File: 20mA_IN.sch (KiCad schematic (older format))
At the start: 10 parts, among them U5 PC817, U6 PC817, U7 LM321

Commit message: Op amp power supply in 20mA_IN switched to 5V
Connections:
- net 24V is gone; now on net 5V: U7.5 (V+)
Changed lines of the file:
@@
 $Descr A4 11693 8268
 encoding utf-8
-Sheet 5 5
+Sheet 4 5
 Title ""
 Date ""
@@
 	6500 4850 6500 4700
 Connection ~ 5950 4850
-Text GLabel 6400 3850 0    50   Input ~ 0
-24V
-Wire Wire Line
-	6400 3850 6500 3850
 Wire Wire Line
 	6500 3850 6500 4100
@@
 	8000 3550 8550 3550
 Connection ~ 8000 3550
+Wire Wire Line
+	5700 3350 5700 3850
+Wire Wire Line
+	5700 3850 6500 3850
 $EndSCHEMATC

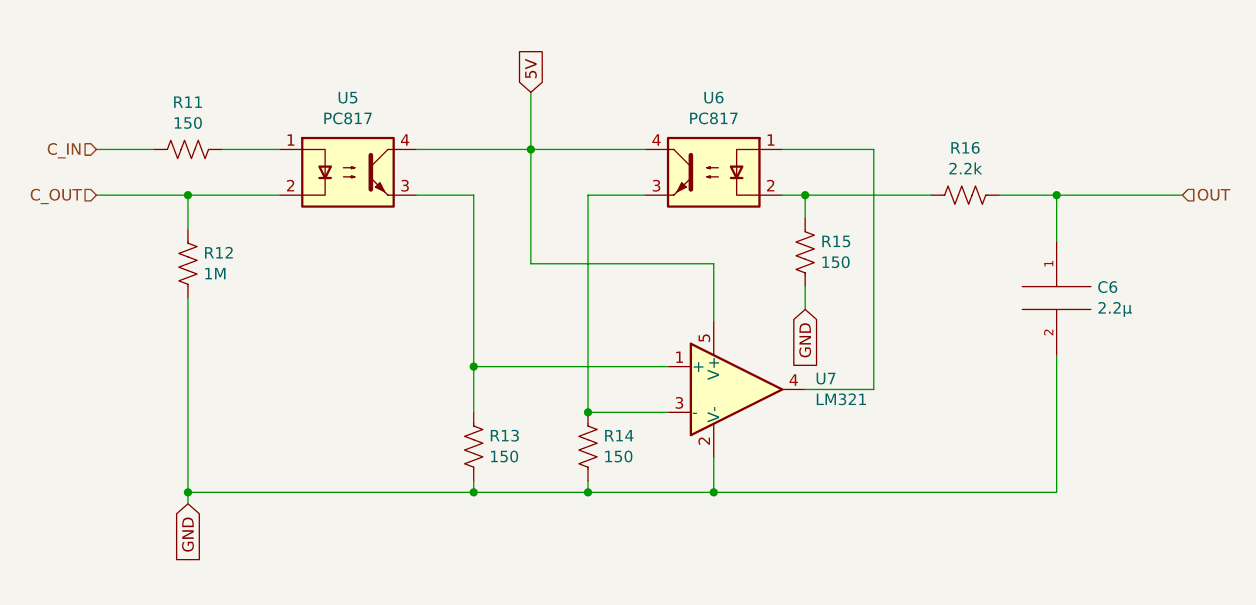
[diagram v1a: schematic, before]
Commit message: Previous current input circuit was reaching op amp saturation. Possible solution may involve transistor, but for now, higher power supply is sufficient.
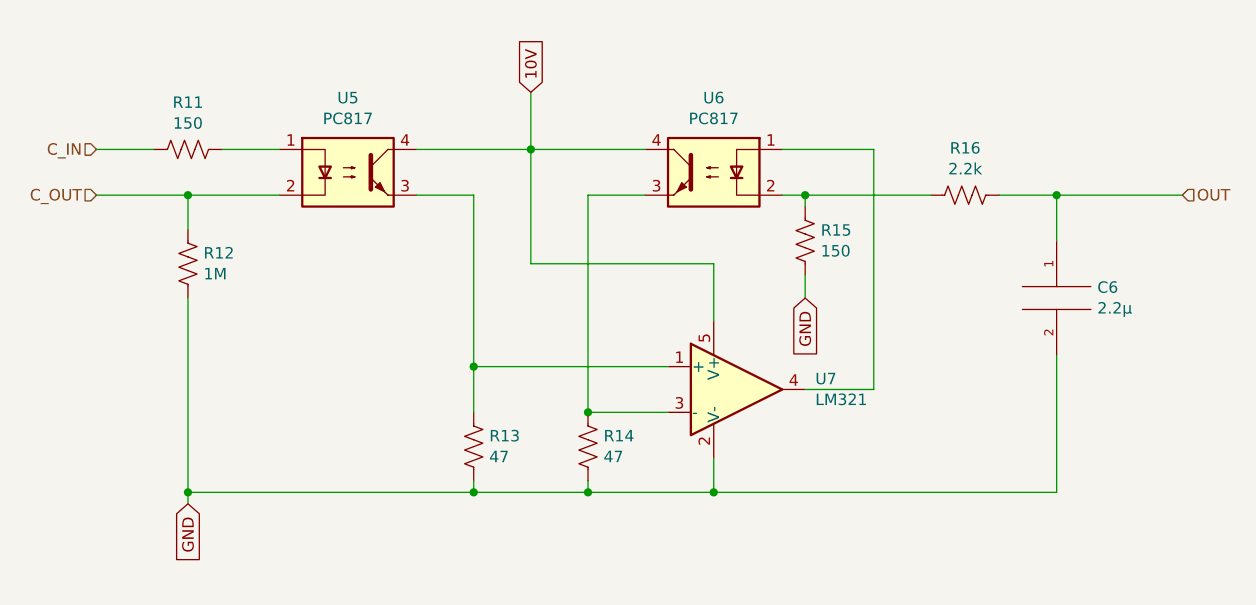
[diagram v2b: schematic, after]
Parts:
- R13, R14: value 150 -> 47
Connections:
- net 5V renamed 10V
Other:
- moved on the sheet: R15
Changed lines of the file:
@@
 P 5950 4650
 F 0 "R14" H 5882 4604 50  0000 R CNN
-F 1 "150" H 5882 4695 50  0000 R CNN
+F 1 "47" H 5882 4695 50  0000 R CNN
 F 2 "" V 5990 4640 50  0001 C CNN
 F 3 "~" H 5950 4650 50  0001 C CNN
@@
 P 5450 4650
 F 0 "R13" H 5382 4604 50  0000 R CNN
-F 1 "150" H 5382 4695 50  0000 R CNN
+F 1 "47" H 5382 4695 50  0000 R CNN
 F 2 "" V 5490 4640 50  0001 C CNN
 F 3 "~" H 5450 4650 50  0001 C CNN
@@
 	4200 4850 4200 4000
 Text GLabel 5700 3100 1    50   Input ~ 0
-5V
+10V
 Wire Wire Line
 	5700 3350 6200 3350
@@
 Wire Wire Line
 	5700 3100 5700 3350
-Wire Wire Line
-	6900 4400 7200 4400
-Wire Wire Line
-	7200 4400 7200 3350
-Wire Wire Line
-	7200 3350 6800 3350
-Text GLabel 6900 4050 3    50   Input ~ 0
+Text GLabel 6900 4000 3    50   Input ~ 0
 GND
-Wire Wire Line
-	6900 3950 6900 4050
-Wire Wire Line
-	6800 3550 6900 3550
-Wire Wire Line
-	6900 3550 6900 3650
 Wire Wire Line
 	5950 4850 6500 4850
@@
 L Device:R_US R15
 U 1 1 60AD8205
-P 6900 3800
-F 0 "R15" H 6832 3754 50  0000 R CNN
-F 1 "150" H 6832 3845 50  0000 R CNN
-F 2 "" V 6940 3790 50  0001 C CNN
-F 3 "~" H 6900 3800 50  0001 C CNN
-	1    6900 3800
+P 6900 3750
+F 0 "R15" H 6832 3704 50  0000 R CNN
+F 1 "150" H 6832 3795 50  0000 R CNN
+F 2 "" V 6940 3740 50  0001 C CNN
+F 3 "~" H 6900 3750 50  0001 C CNN
+	1    6900 3750
 	-1   0    0    1
 $EndComp
@@
 $EndComp
 Wire Wire Line
-	6900 3550 7450 3550
-Connection ~ 6900 3550
-Wire Wire Line
 	7750 3550 8000 3550
 Wire Wire Line
@@
 Wire Wire Line
 	5700 3850 6500 3850
+Wire Wire Line
+	6800 3550 6900 3550
+Wire Wire Line
+	6900 3550 6900 3600
+Connection ~ 6900 3550
+Wire Wire Line
+	6900 3550 7450 3550
+Wire Wire Line
+	6900 4400 7200 4400
+Wire Wire Line
+	7200 4400 7200 3350
+Wire Wire Line
+	7200 3350 6800 3350
+Wire Wire Line
+	6900 3900 6900 4000
 $EndSCHEMATC

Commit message: Added Optically Isolated Digital Input
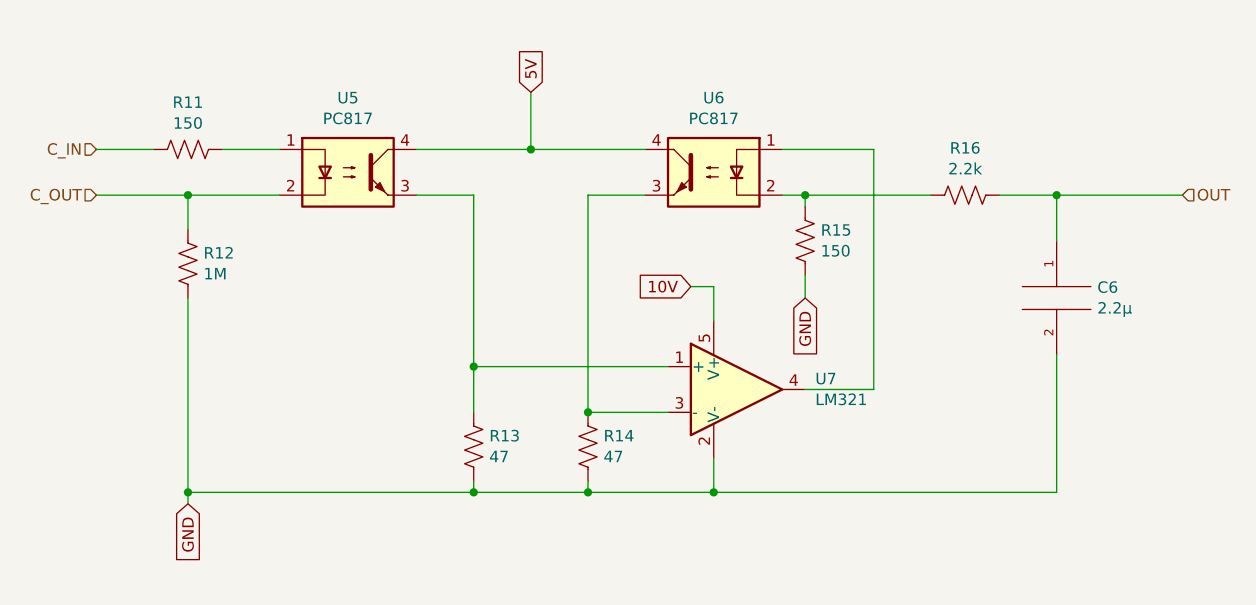
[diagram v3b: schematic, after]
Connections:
- net 10V: no longer U5.4, U6.4
- new net 5V: U5.4, U6.4
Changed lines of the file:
@@
 $Descr A4 11693 8268
 encoding utf-8
-Sheet 4 5
+Sheet 5 6
 Title ""
 Date ""
@@
 	4200 4850 4200 4000
 Text GLabel 5700 3100 1    50   Input ~ 0
-10V
+5V
 Wire Wire Line
 	5700 3350 6200 3350
@@
 	6500 4850 6500 4700
 Connection ~ 5950 4850
-Wire Wire Line
-	6500 3850 6500 4100
 $Comp
 L Device:R_US R15
@@
 Connection ~ 8000 3550
 Wire Wire Line
-	5700 3350 5700 3850
-Wire Wire Line
-	5700 3850 6500 3850
-Wire Wire Line
 	6800 3550 6900 3550
 Wire Wire Line
@@
 Wire Wire Line
 	6900 3900 6900 4000
+Text GLabel 6400 3950 0    50   Input ~ 0
+10V
+Wire Wire Line
+	6400 3950 6500 3950
+Wire Wire Line
+	6500 3950 6500 4100
 $EndSCHEMATC

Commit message: Comments and Notation for clarity
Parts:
- added Q?: S8050, Package_TO_SOT_THT:TO-92_Inline, symbol Transistor_BJT:S8050
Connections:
- net 10V is gone; now on net 5V: U7.5 (V+)
- net 5V: now also Q?.3 (C)
- net at U6.1: now also Q?.1 (E); no longer U7.4
- new net: Q?.2 (B), U7.4
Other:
- note added: "1st Order Low Pass Filter"
- note added: "Since V over R13 = V over R14 by presence of U7, I into U5 = I into U6"
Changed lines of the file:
@@
 encoding utf-8
 Sheet 5 6
-Title ""
-Date ""
-Rev ""
-Comp ""
-Comment1 ""
+Title "20mA to 3.3V Input"
+Date "2021-05-25"
+Rev "1"
+Comp "Harsch Systems"
+Comment1 "Tyler Stowell"
 Comment2 ""
 Comment3 ""
@@
 $EndComp
 $Comp
-L Amplifier_Operational:LM321 U?
-U 1 1 60ACD8A3
-P 6600 4400
-AR Path="/60A68B69/60ACD8A3" Ref="U?"  Part="1"
-AR Path="/60A8EFC5/60ACD8A3" Ref="U?"  Part="1"
-AR Path="/60AC3F67/60ACD8A3" Ref="U7"  Part="1"
-F 0 "U7" H 6944 4446 50  0000 L CNN
-F 1 "LM321" H 6944 4355 50  0000 L CNN
-F 2 "Package_TO_SOT_SMD:SOT-23-5" H 6600 4400 50  0001 C CNN
-F 3 "http://www.ti.com/lit/ds/symlink/lm321.pdf" H 6600 4400 50  0001 C CNN
-	1    6600 4400
-	1    0    0    -1
-$EndComp
-$Comp
 L Device:R_US R14
 U 1 1 60ACED9B
@@
 Wire Wire Line
 	5700 3100 5700 3350
-Text GLabel 6900 4000 3    50   Input ~ 0
+Text GLabel 6850 3950 0    50   Input ~ 0
 GND
 Wire Wire Line
@@
 	6900 3550 6900 3600
 Connection ~ 6900 3550
+Text GLabel 6400 3950 0    50   Input ~ 0
+5V
+Wire Wire Line
+	6400 3950 6500 3950
+Text Notes 7600 5250 2    50   ~ 0
+Since V over R13 = V over R14 by presence of U7, I into U5 = I into U6
+Wire Notes Line
+	7400 3250 8400 3250
+Wire Notes Line
+	8400 3250 8400 4300
+Wire Notes Line
+	8400 4300 7400 4300
+Wire Notes Line
+	7400 4300 7400 3250
+Text Notes 8400 3200 2    50   ~ 0
+1st Order Low Pass Filter
+Wire Wire Line
+	6900 3900 6900 3950
+Wire Wire Line
+	6900 3950 6850 3950
+Wire Wire Line
+	6500 3950 6500 4100
+$Comp
+L Amplifier_Operational:LM321 U?
+U 1 1 60ACD8A3
+P 6600 4400
+AR Path="/60A68B69/60ACD8A3" Ref="U?"  Part="1"
+AR Path="/60A8EFC5/60ACD8A3" Ref="U?"  Part="1"
+AR Path="/60AC3F67/60ACD8A3" Ref="U7"  Part="1"
+F 0 "U7" H 6700 4300 50  0000 L CNN
+F 1 "LM321" H 6700 4200 50  0000 L CNN
+F 2 "Package_TO_SOT_SMD:SOT-23-5" H 6600 4400 50  0001 C CNN
+F 3 "http://www.ti.com/lit/ds/symlink/lm321.pdf" H 6600 4400 50  0001 C CNN
+	1    6600 4400
+	1    0    0    -1
+$EndComp
+Wire Wire Line
+	6900 4400 7050 4400
+Wire Wire Line
+	6500 4100 6850 4100
+Connection ~ 6500 4100
+$Comp
+L Transistor_BJT:S8050 Q?
+U 1 1 60B7546B
+P 7050 4200
+F 0 "Q?" V 7350 4200 50  0000 C CNN
+F 1 "S8050" V 7250 4200 50  0000 C CNN
+F 2 "Package_TO_SOT_THT:TO-92_Inline" H 7250 4125 50  0001 L CIN
+F 3 "http://www.unisonic.com.tw/datasheet/S8050.pdf" H 7050 4200 50  0001 L CNN
+	1    7050 4200
+	0    -1   -1   0
+$EndComp
 Wire Wire Line
 	6900 3550 7450 3550
 Wire Wire Line
-	6900 4400 7200 4400
-Wire Wire Line
-	7200 4400 7200 3350
-Wire Wire Line
-	7200 3350 6800 3350
-Wire Wire Line
-	6900 3900 6900 4000
-Text GLabel 6400 3950 0    50   Input ~ 0
-10V
-Wire Wire Line
-	6400 3950 6500 3950
-Wire Wire Line
-	6500 3950 6500 4100
+	7250 4100 7250 3350
+Wire Wire Line
+	7250 3350 6800 3350
 $EndSCHEMATC

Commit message: Cleanup, added second digital input, and created sheet for digital output (currently empty)
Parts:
- removed Q?: S8050, Package_TO_SOT_THT:TO-92_Inline, symbol Transistor_BJT:S8050
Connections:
- net 5V: no longer U7.5 (V+)
- net at U6.1: now also U7.4
- new net 24V: U7.5 (V+)
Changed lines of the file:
@@
 $Descr A4 11693 8268
 encoding utf-8
-Sheet 5 6
+Sheet 5 7
 Title "20mA to 3.3V Input"
 Date "2021-05-25"
@@
 Connection ~ 6900 3550
 Text GLabel 6400 3950 0    50   Input ~ 0
-5V
+24V
 Wire Wire Line
 	6400 3950 6500 3950
@@
 $EndComp
 Wire Wire Line
-	6900 4400 7050 4400
-Wire Wire Line
-	6500 4100 6850 4100
-Connection ~ 6500 4100
-$Comp
-L Transistor_BJT:S8050 Q?
-U 1 1 60B7546B
-P 7050 4200
-F 0 "Q?" V 7350 4200 50  0000 C CNN
-F 1 "S8050" V 7250 4200 50  0000 C CNN
-F 2 "Package_TO_SOT_THT:TO-92_Inline" H 7250 4125 50  0001 L CIN
-F 3 "http://www.unisonic.com.tw/datasheet/S8050.pdf" H 7050 4200 50  0001 L CNN
-	1    7050 4200
-	0    -1   -1   0
-$EndComp
-Wire Wire Line
 	6900 3550 7450 3550
 Wire Wire Line
-	7250 4100 7250 3350
-Wire Wire Line
 	7250 3350 6800 3350
+Wire Wire Line
+	6900 4400 7250 4400
+Wire Wire Line
+	7250 4400 7250 3350
 $EndSCHEMATC

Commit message: Testing and adjustments
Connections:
- net 5V renamed 3.3V
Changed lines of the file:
@@
 $Descr A4 11693 8268
 encoding utf-8
-Sheet 5 7
+Sheet 5 8
 Title "20mA to 3.3V Input"
 Date "2021-05-25"
@@
 	4200 4850 4200 4000
 Text GLabel 5700 3100 1    50   Input ~ 0
-5V
+3.3V
 Wire Wire Line
 	5700 3350 6200 3350

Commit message: Footprint Association
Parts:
- removed U7: LM321, Package_TO_SOT_SMD:SOT-23-5, symbol Amplifier_Operational:LM321
- added U2: LM324, Package_DIP:DIP-14_W7.62mm, symbol Amplifier_Operational:LM324
- C6: footprint (none) -> Capacitor_THT:C_Disc_D5.1mm_W3.2mm_P5.00mm
- R11, R12, R13, R14, R15, R16: footprint (none) -> Resistor_THT:R_Axial_DIN0207_L6.3mm_D2.5mm_P10.16mm_Horizontal
- renumbered U5 to U3, U6 to U4
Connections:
- net at R13.2, U3.3: now also U2.10 (+)
- net at U4.1: now also U2.8
- net at R14.2, U4.3: now also U2.9 (-)
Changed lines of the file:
@@
 F 0 "R11" V 3995 3350 50  0000 C CNN
 F 1 "150" V 4086 3350 50  0000 C CNN
-F 2 "" V 4240 3340 50  0001 C CNN
+F 2 "Resistor_THT:R_Axial_DIN0207_L6.3mm_D2.5mm_P10.16mm_Horizontal" V 4240 3340 50  0001 C CNN
 F 3 "~" H 4200 3350 50  0001 C CNN
 	1    4200 3350
@@
 F 0 "R12" H 4132 3804 50  0000 R CNN
 F 1 "1M" H 4132 3895 50  0000 R CNN
-F 2 "" V 4240 3840 50  0001 C CNN
+F 2 "Resistor_THT:R_Axial_DIN0207_L6.3mm_D2.5mm_P10.16mm_Horizontal" V 4240 3840 50  0001 C CNN
 F 3 "~" H 4200 3850 50  0001 C CNN
 	1    4200 3850
@@
 $EndComp
 $Comp
-L Isolator:PC817 U5
+L Isolator:PC817 U3
 U 1 1 60AC7AD1
 P 4900 3450
-F 0 "U5" H 4900 3775 50  0000 C CNN
+F 0 "U3" H 4900 3775 50  0000 C CNN
 F 1 "PC817" H 4900 3684 50  0000 C CNN
 F 2 "Package_DIP:DIP-4_W7.62mm" H 4700 3250 50  0001 L CIN
@@
 GND
 $Comp
-L Isolator:PC817 U6
+L Isolator:PC817 U4
 U 1 1 60ACAAFE
 P 6500 3450
-F 0 "U6" H 6500 3775 50  0000 C CNN
+F 0 "U4" H 6500 3775 50  0000 C CNN
 F 1 "PC817" H 6500 3684 50  0000 C CNN
 F 2 "Package_DIP:DIP-4_W7.62mm" H 6300 3250 50  0001 L CIN
@@
 F 0 "R14" H 5882 4604 50  0000 R CNN
 F 1 "47" H 5882 4695 50  0000 R CNN
-F 2 "" V 5990 4640 50  0001 C CNN
+F 2 "Resistor_THT:R_Axial_DIN0207_L6.3mm_D2.5mm_P10.16mm_Horizontal" V 5990 4640 50  0001 C CNN
 F 3 "~" H 5950 4650 50  0001 C CNN
 	1    5950 4650
@@
 F 0 "R13" H 5382 4604 50  0000 R CNN
 F 1 "47" H 5382 4695 50  0000 R CNN
-F 2 "" V 5490 4640 50  0001 C CNN
+F 2 "Resistor_THT:R_Axial_DIN0207_L6.3mm_D2.5mm_P10.16mm_Horizontal" V 5490 4640 50  0001 C CNN
 F 3 "~" H 5450 4650 50  0001 C CNN
 	1    5450 4650
@@
 Text GLabel 6850 3950 0    50   Input ~ 0
 GND
-Wire Wire Line
-	5950 4850 6500 4850
-Wire Wire Line
-	6500 4850 6500 4700
 Connection ~ 5950 4850
 $Comp
@@
 F 0 "R15" H 6832 3704 50  0000 R CNN
 F 1 "150" H 6832 3795 50  0000 R CNN
-F 2 "" V 6940 3740 50  0001 C CNN
+F 2 "Resistor_THT:R_Axial_DIN0207_L6.3mm_D2.5mm_P10.16mm_Horizontal" V 6940 3740 50  0001 C CNN
 F 3 "~" H 6900 3750 50  0001 C CNN
 	1    6900 3750
@@
 F 0 "R16" V 7395 3550 50  0000 C CNN
 F 1 "2.2k" V 7486 3550 50  0000 C CNN
-F 2 "" V 7640 3540 50  0001 C CNN
+F 2 "Resistor_THT:R_Axial_DIN0207_L6.3mm_D2.5mm_P10.16mm_Horizontal" V 7640 3540 50  0001 C CNN
 F 3 "~" H 7600 3550 50  0001 C CNN
 	1    7600 3550
@@
 F 0 "C6" H 8178 4046 50  0000 L CNN
 F 1 "2.2µ" H 8178 3955 50  0000 L CNN
-F 2 "" H 8000 4000 50  0001 C CNN
+F 2 "Capacitor_THT:C_Disc_D5.1mm_W3.2mm_P5.00mm" H 8000 4000 50  0001 C CNN
 F 3 "~" H 8000 4000 50  0001 C CNN
 	1    8000 4000
@@
 	8000 3550 8000 3750
 Wire Wire Line
-	6500 4850 8000 4850
-Wire Wire Line
 	8000 4850 8000 4250
-Connection ~ 6500 4850
 Text HLabel 8550 3550 2    50   Input ~ 0
 OUT
@@
 	6900 3550 6900 3600
 Connection ~ 6900 3550
-Text GLabel 6400 3950 0    50   Input ~ 0
-24V
-Wire Wire Line
-	6400 3950 6500 3950
 Text Notes 7600 5250 2    50   ~ 0
 Since V over R13 = V over R14 by presence of U7, I into U5 = I into U6
@@
 	6900 3950 6850 3950
 Wire Wire Line
-	6500 3950 6500 4100
-$Comp
-L Amplifier_Operational:LM321 U?
-U 1 1 60ACD8A3
+	6900 3550 7450 3550
+Wire Wire Line
+	7250 3350 6800 3350
+Wire Wire Line
+	6900 4400 7250 4400
+Wire Wire Line
+	7250 4400 7250 3350
+Wire Wire Line
+	5950 4850 8000 4850
+$Comp
+L Amplifier_Operational:LM324 U2
+U 3 1 60C6761C
 P 6600 4400
-AR Path="/60A68B69/60ACD8A3" Ref="U?"  Part="1"
-AR Path="/60A8EFC5/60ACD8A3" Ref="U?"  Part="1"
-AR Path="/60AC3F67/60ACD8A3" Ref="U7"  Part="1"
-F 0 "U7" H 6700 4300 50  0000 L CNN
-F 1 "LM321" H 6700 4200 50  0000 L CNN
-F 2 "Package_TO_SOT_SMD:SOT-23-5" H 6600 4400 50  0001 C CNN
-F 3 "http://www.ti.com/lit/ds/symlink/lm321.pdf" H 6600 4400 50  0001 C CNN
-	1    6600 4400
+F 0 "U2" H 6600 4767 50  0000 C CNN
+F 1 "LM324" H 6600 4676 50  0000 C CNN
+F 2 "Package_DIP:DIP-14_W7.62mm" H 6550 4500 50  0001 C CNN
+F 3 "http://www.ti.com/lit/ds/symlink/lm2902-n.pdf" H 6650 4600 50  0001 C CNN
+	3    6600 4400
 	1    0    0    -1
 $EndComp
-Wire Wire Line
-	6900 3550 7450 3550
-Wire Wire Line
-	7250 3350 6800 3350
-Wire Wire Line
-	6900 4400 7250 4400
-Wire Wire Line
-	7250 4400 7250 3350
 $EndSCHEMATC

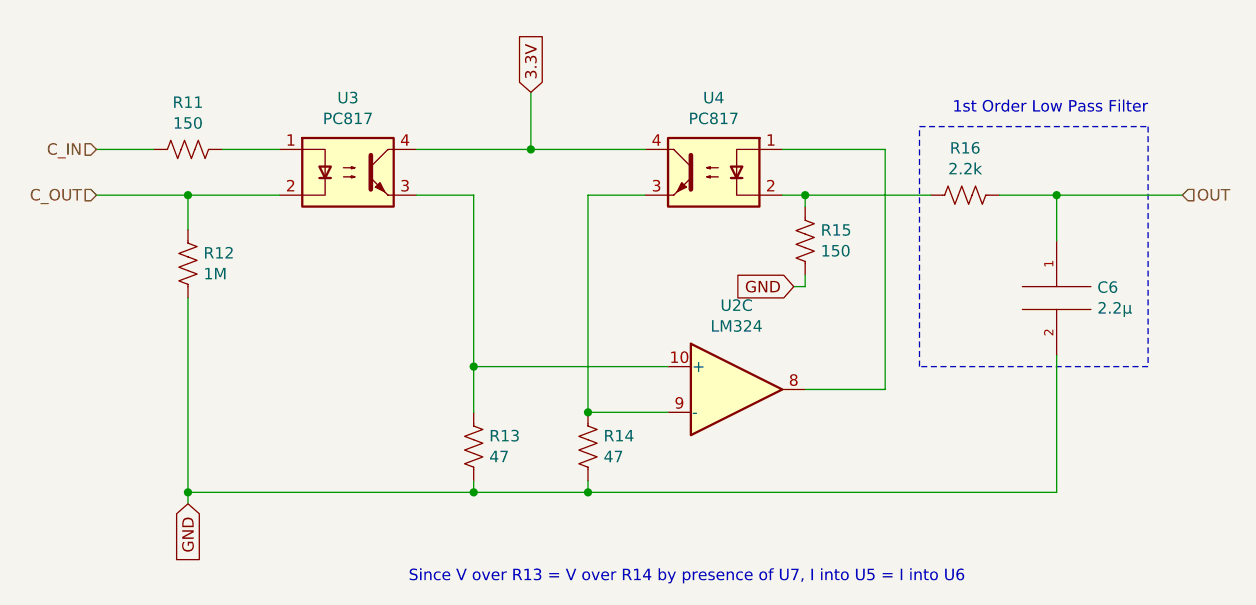
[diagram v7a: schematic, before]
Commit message: Fixed a couple of discrepancies between my test circuit and the schematic
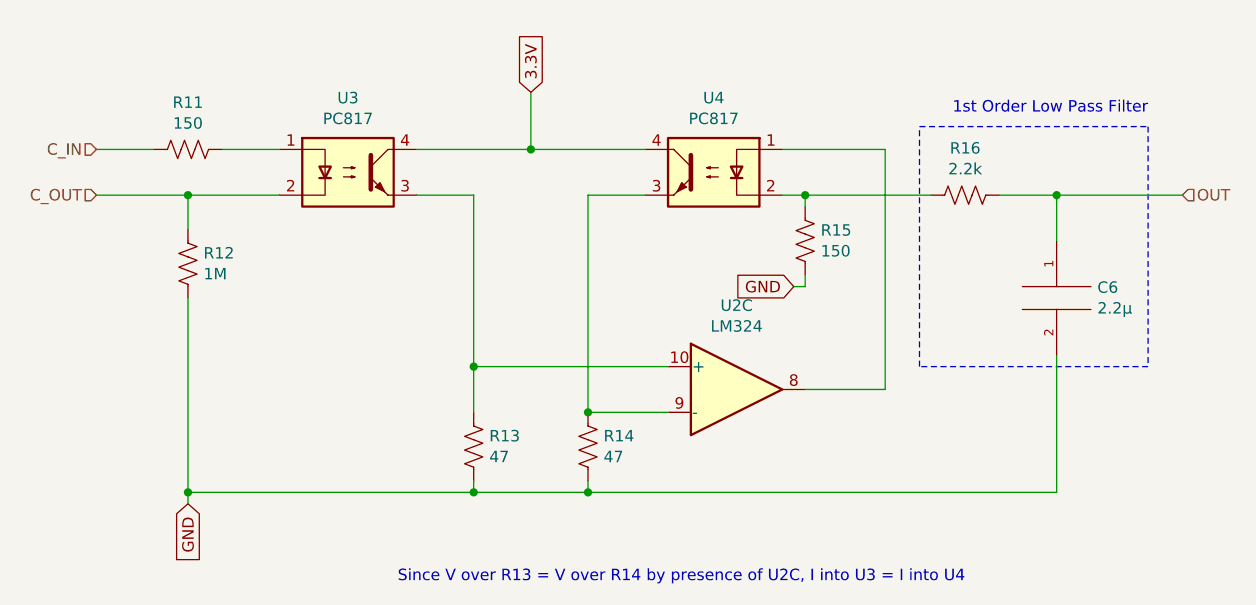
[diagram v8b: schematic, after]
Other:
- note added: "Since V over R13 = V over R14 by presence of U2C, I into U3 = I into U4"
- note removed: "Since V over R13 = V over R14 by presence of U7, I into U5 = I into U6"
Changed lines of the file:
@@
 Connection ~ 6900 3550
 Text Notes 7600 5250 2    50   ~ 0
-Since V over R13 = V over R14 by presence of U7, I into U5 = I into U6
+Since V over R13 = V over R14 by presence of U2C, I into U3 = I into U4
 Wire Notes Line
 	7400 3250 8400 3250
